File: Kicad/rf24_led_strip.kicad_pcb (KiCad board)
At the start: 2 copper layers, 50 x 50 mm, 91 parts, among them P1 12V in, P10 CONN_01X04, P11 CONN_01X07, P2 LED_OUT, P3 LED2_OUT, P4 LED3_OUT, P5 LED4_OUT, P6 LED5_OUT, P7 USB_OTG, P8 SWD, P9 UART, Q10 Q_NMOS_GDS, Q11 Q_NMOS_GDS, Q12 Q_NMOS_GDS, Q13 Q_NMOS_GDS, Q14 Q_NMOS_GDS, Q15 Q_NMOS_GDS, Q16 Q_NMOS_GDS, Q2 Q_NMOS_GDS, Q3 Q_NMOS_GDS, Q4 Q_NMOS_GDS, Q5 Q_NMOS_GDS, Q6 Q_NMOS_GDS, Q7 Q_NMOS_GDS, Q8 Q_NMOS_GDS, Q9 Q_NMOS_GDS, U1 nrf24l01+, U2 ESP-01, U3 STM32F103C8Tx, U4 AMS1117, Y1 Crystal

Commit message: Update power supply.
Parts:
- added C3: 10µF, Capacitors_SMD:C_0805, F.Cu at (106.4, 58.5)
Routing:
- net +3V3: track 123.5 -> 187.0 mm, vias 2 -> 24
- net GND: track 82.8 -> 88.6 mm, vias 21 -> 22
- net /NRST: track 21.8 -> 22.5 mm
- added copper zone on B.Cu, net +3V3
- added copper zone on F.Cu, net +3V3
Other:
- net class Dick: via_dia 0.6 -> 1.2; via_drill 0.4 -> 0.8

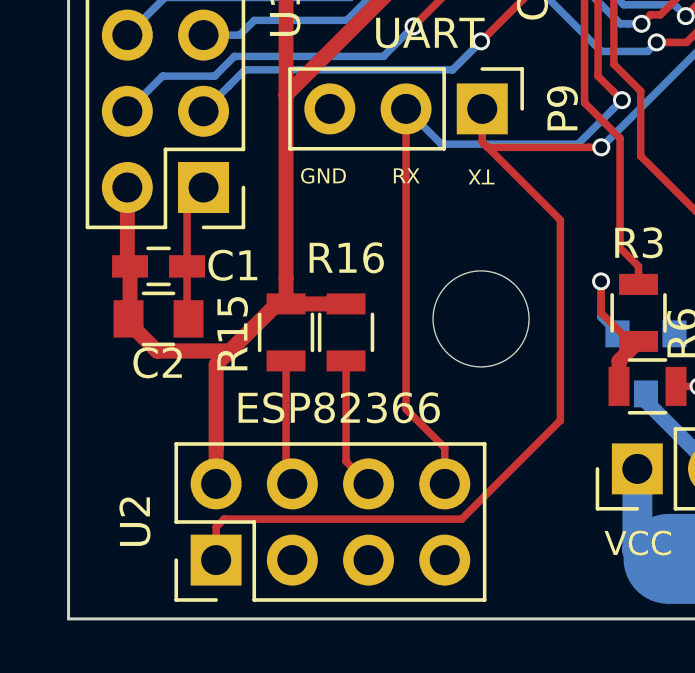
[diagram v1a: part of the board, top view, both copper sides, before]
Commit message: Add capacitors to the ESP8266.
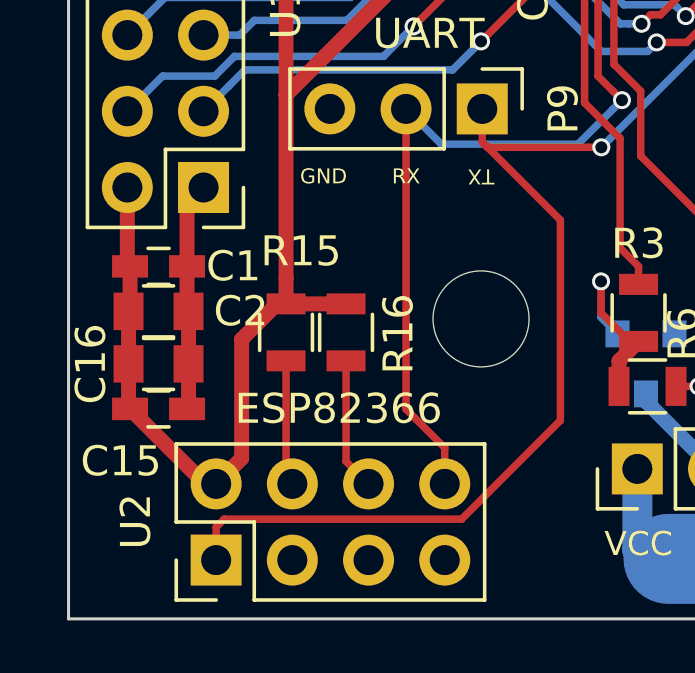
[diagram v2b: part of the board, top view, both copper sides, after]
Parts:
- added C15: 100nF, Capacitors_SMD:C_0603_HandSoldering, F.Cu at (103.0, 93.0)
- added C16: 10µF, Capacitors_SMD:C_0805, F.Cu at (103.0, 91.5)
- moved REF*** 1.00 mm to (113.0, 56.5)
- moved C2 0.25 mm to (103.0, 89.8)
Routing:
- net +3V3: track 187.0 -> 180.7 mm
- net GND: track 88.6 -> 91.7 mm
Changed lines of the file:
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@@
 (kicad_pcb (version 4) (host pcbnew 4.0.5)
   (general
-    (links 194)
-    (no_connects 0)
+    (links 198)
+    (no_connects 2)
     (area 99.949999 49.949999 150.050001 100.050001)
     (thickness 1.6)
     (drawings 52)
-    (tracks 775)
+    (tracks 777)
     (zones 0)
-    (modules 92)
+    (modules 94)
     (nets 79)
   )
@@
   )
   (setup
-    (last_trace_width 0.25)
+    (last_trace_width 0.5)
     (user_trace_width 0.25)
     (user_trace_width 0.5)
@@
     (tags "resistor 0805")
     (attr smd)
-    (fp_text reference R15 (at -0.05 -1.75 270) (layer F.SilkS)
+    (fp_text reference R15 (at 2.7 0.5 360) (layer F.SilkS)
       (effects (font (size 1 1) (thickness 0.15)))
     )
@@
     (tags "resistor 0805")
     (attr smd)
-    (fp_text reference R16 (at 2.45 0 180) (layer F.SilkS)
+    (fp_text reference R16 (at -0.05 1.75 90) (layer F.SilkS)
       (effects (font (size 1 1) (thickness 0.15)))
     )
@@
   )
   (module Capacitors_SMD:C_0805 (layer F.Cu)
-    (at 103 90)
+    (at 103 89.75)
     (descr "Capacitor SMD 0805, reflow soldering, AVX (see smccp.pdf)")
     (tags "capacitor 0805")
     (attr smd)
-    (fp_text reference C2 (at 0 1.5) (layer F.SilkS)
+    (fp_text reference C2 (at 2.75 0) (layer F.SilkS)
       (effects (font (size 1 1) (thickness 0.15)))
     )
@@
   )
   (module Symbols:OSHW-Logo2_14.6x12mm_SilkScreen (layer B.Cu)
-    (at 114 56.5)
+    (at 113 56.5)
     (descr "Open Source Hardware Symbol")
     (tags "Logo Symbol OSHW")
@@
     )
   )
+  (module Capacitors_SMD:C_0603_HandSoldering (layer F.Cu)
+    (at 103 93)
+    (descr "Capacitor SMD 0603, hand soldering")
+    (tags "capacitor 0603")
+    (attr smd)
+    (fp_text reference C15 (at -1.25 1.75) (layer F.SilkS)
+      (effects (font (size 1 1) (thickness 0.15)))
+    )
+    (fp_text value 100nF (at 0 1.5) (layer F.Fab)
+      (effects (font (size 1 1) (thickness 0.15)))
+    )
+    (fp_text user %R (at 0 -1.25) (layer F.Fab)
+      (effects (font (size 1 1) (thickness 0.15)))
+    )
+    (fp_line (start -0.8 0.4) (end -0.8 -0.4) (layer F.Fab) (width 0.1))
+    (fp_line (start 0.8 0.4) (end -0.8 0.4) (layer F.Fab) (width 0.1))
+    (fp_line (start 0.8 -0.4) (end 0.8 0.4) (layer F.Fab) (width 0.1))
+    (fp_line (start -0.8 -0.4) (end 0.8 -0.4) (layer F.Fab) (width 0.1))
+    (fp_line (start -0.35 -0.6) (end 0.35 -0.6) (layer F.SilkS) (width 0.12))
+    (fp_line (start 0.35 0.6) (end -0.35 0.6) (layer F.SilkS) (width 0.12))
+    (fp_line (start -1.8 -0.65) (end 1.8 -0.65) (layer F.CrtYd) (width 0.05))
+    (fp_line (start -1.8 -0.65) (end -1.8 0.65) (layer F.CrtYd) (width 0.05))
+    (fp_line (start 1.8 0.65) (end 1.8 -0.65) (layer F.CrtYd) (width 0.05))
+    (fp_line (start 1.8 0.65) (end -1.8 0.65) (layer F.CrtYd) (width 0.05))
+    (pad 1 smd rect (at -0.95 0) (size 1.2 0.75) (layers F.Cu F.Paste F.Mask)
+      (net 3 +3V3))
+    (pad 2 smd rect (at 0.95 0) (size 1.2 0.75) (layers F.Cu F.Paste F.Mask)
+      (net 1 GND))
+    (model Capacitors_SMD.3dshapes/C_0603.wrl
+      (at (xyz 0 0 0))
+      (scale (xyz 1 1 1))
+      (rotate (xyz 0 0 0))
+    )
+  )
+  (module Capacitors_SMD:C_0805 (layer F.Cu)
+    (at 103 91.5)
+    (descr "Capacitor SMD 0805, reflow soldering, AVX (see smccp.pdf)")
+    (tags "capacitor 0805")
+    (attr smd)
+    (fp_text reference C16 (at -2.25 0 270) (layer F.SilkS)
+      (effects (font (size 1 1) (thickness 0.15)))
+    )
+    (fp_text value 10µF (at 0 1.75) (layer F.Fab)
+      (effects (font (size 1 1) (thickness 0.15)))
+    )
+    (fp_text user %R (at 0 -1.5) (layer F.Fab)
+      (effects (font (size 1 1) (thickness 0.15)))
+    )
+    (fp_line (start -1 0.62) (end -1 -0.62) (layer F.Fab) (width 0.1))
+    (fp_line (start 1 0.62) (end -1 0.62) (layer F.Fab) (width 0.1))
+    (fp_line (start 1 -0.62) (end 1 0.62) (layer F.Fab) (width 0.1))
+    (fp_line (start -1 -0.62) (end 1 -0.62) (layer F.Fab) (width 0.1))
+    (fp_line (start 0.5 -0.85) (end -0.5 -0.85) (layer F.SilkS) (width 0.12))
+    (fp_line (start -0.5 0.85) (end 0.5 0.85) (layer F.SilkS) (width 0.12))
+    (fp_line (start -1.75 -0.88) (end 1.75 -0.88) (layer F.CrtYd) (width 0.05))
+    (fp_line (start -1.75 -0.88) (end -1.75 0.87) (layer F.CrtYd) (width 0.05))
+    (fp_line (start 1.75 0.87) (end 1.75 -0.88) (layer F.CrtYd) (width 0.05))
+    (fp_line (start 1.75 0.87) (end -1.75 0.87) (layer F.CrtYd) (width 0.05))
+    (pad 1 smd rect (at -1 0) (size 1 1.25) (layers F.Cu F.Paste F.Mask)
+      (net 3 +3V3))
+    (pad 2 smd rect (at 1 0) (size 1 1.25) (layers F.Cu F.Paste F.Mask)
+      (net 1 GND))
+    (model Capacitors_SMD.3dshapes/C_0805.wrl
+      (at (xyz 0 0 0))
+      (scale (xyz 1 1 1))
+      (rotate (xyz 0 0 0))
+    )
+  )
   (gr_text 4 (at 134.75 78.5 90) (layer F.SilkS)
     (effects (font (size 0.8 0.8) (thickness 0.15)))
@@
     (arrow2b (pts (xy 100 45) (xy 101.126504 44.413579)))
   )
+  (segment (start 104 91.5) (end 104 92.95) (width 0.5) (layer F.Cu) (net 1))
+  (segment (start 104 92.95) (end 103.95 93) (width 0.5) (layer F.Cu) (net 1))
+  (segment (start 104 89.75) (end 104 91.5) (width 0.5) (layer F.Cu) (net 1))
+  (segment (start 103.95 88.25) (end 103.95 89.7) (width 0.5) (layer F.Cu) (net 1))
+  (segment (start 103.95 89.7) (end 104 89.75) (width 0.5) (layer F.Cu) (net 1))
+  (segment (start 103.95 88.25) (end 103.95 86.17) (width 0.5) (layer F.Cu) (net 1))
+  (segment (start 103.95 86.17) (end 104.5 85.62) (width 0.5) (layer F.Cu) (net 1))
+  (segment (start 104 88.3) (end 103.95 88.25) (width 0.5) (layer F.Cu) (net 1))
   (segment (start 117.9 74.5) (end 119.5 74.5) (width 0.25) (layer F.Cu) (net 1))
   (via (at 120 74) (size 0.6) (drill 0.4) (layers F.Cu B.Cu) (net 1))
@@
   (segment (start 124.5 76.719689) (end 124.331423 76.551112) (width 0.25) (layer F.Cu) (net 1))
   (segment (start 124.331423 76.551112) (end 124.031424 76.251113) (width 0.25) (layer F.Cu) (net 1))
-  (segment (start 103.95 88.25) (end 103.95 89.95) (width 0.25) (layer F.Cu) (net 1))
-  (segment (start 103.95 89.95) (end 104 90) (width 0.25) (layer F.Cu) (net 1))
-  (segment (start 103.95 88.25) (end 103.95 86.17) (width 0.25) (layer F.Cu) (net 1))
-  (segment (start 103.95 86.17) (end 104.5 85.62) (width 0.25) (layer F.Cu) (net 1))
   (segment (start 119.7 60.5) (end 119.7 56.7) (width 0.5) (layer F.Cu) (net 1))
   (segment (start 119.7 56.7) (end 119.5 56.5) (width 0.5) (layer F.Cu) (net 1))
@@
   (segment (start 118.96 95) (end 118.96 97.71) (width 1) (layer B.Cu) (net 2))
   (segment (start 118.96 97.71) (end 119.25 98) (width 1) (layer B.Cu) (net 2))
+  (segment (start 104.92 95.5) (end 105.769999 94.650001) (width 0.5) (layer F.Cu) (net 3))
+  (segment (start 105.769999 94.650001) (end 105.769999 90.680001) (width 0.5) (layer F.Cu) (net 3))
+  (segment (start 105.769999 90.680001) (end 106.95 89.5) (width 0.5) (layer F.Cu) (net 3))
+  (segment (start 106.95 89.5) (end 107.25 89.5) (width 0.5) (layer F.Cu) (net 3))
+  (segment (start 102.05 93) (end 104.55 95.5) (width 0.5) (layer F.Cu) (net 3))
+  (segment (start 104.55 95.5) (end 104.92 95.5) (width 0.5) (layer F.Cu) (net 3))
+  (segment (start 102 91.5) (end 102 92.95) (width 0.5) (layer F.Cu) (net 3))
+  (segment (start 102 92.95) (end 102.05 93) (width 0.5) (layer F.Cu) (net 3))
+  (segment (start 102 89.75) (end 102 91.5) (width 0.5) (layer F.Cu) (net 3))
+  (segment (start 102.05 88.25) (end 102.05 89.7) (width 0.5) (layer F.Cu) (net 3))
+  (segment (start 102.05 89.7) (end 102 89.75) (width 0.5) (layer F.Cu) (net 3))
   (segment (start 119.175004 70.75) (end 119.05 70.75) (width 0.25) (layer F.Cu) (net 3))
   (segment (start 120.75 74) (end 120.75 72.324996) (width 0.25) (layer F.Cu) (net 3))
@@
   (segment (start 110 62.75) (end 109.549999 63.200001) (width 0.5) (layer B.Cu) (net 3))
   (via (at 107.25 75) (size 1.2) (drill 0.8) (layers F.Cu B.Cu) (net 3))
-  (segment (start 107.25 89.5) (end 106.95 89.5) (width 0.5) (layer F.Cu) (net 3))
-  (segment (start 104.92 91.53) (end 104.92 94.297919) (width 0.5) (layer F.Cu) (net 3))
-  (segment (start 106.95 89.5) (end 104.92 91.53) (width 0.5) (layer F.Cu) (net 3))
-  (segment (start 104.92 94.297919) (end 104.92 95.5) (width 0.5) (layer F.Cu) (net 3))
   (segment (start 102 90) (end 102 90.125) (width 0.5) (layer F.Cu) (net 3))
-  (segment (start 102 90.125) (end 102.950001 91.075001) (width 0.5) (layer F.Cu) (net 3))
-  (segment (start 102.950001 91.075001) (end 105.374999 91.075001) (width 0.5) (layer F.Cu) (net 3))
-  (segment (start 105.374999 91.075001) (end 106.95 89.5) (width 0.5) (layer F.Cu) (net 3))
-  (segment (start 102.05 88.25) (end 102.05 89.95) (width 0.5) (layer F.Cu) (net 3))
   (segment (start 102.05 89.95) (end 102 90) (width 0.5) (layer F.Cu) (net 3))
   (segment (start 101.96 85.62) (end 101.96 88.16) (width 0.5) (layer F.Cu) (net 3))
@@
   (segment (start 109.65 60.75) (end 109 60.75) (width 0.25) (layer F.Cu) (net 3))
   (via (at 109 60.75) (size 0.6) (drill 0.4) (layers F.Cu B.Cu) (net 3))
-  (segment (start 105.499999 90.950001) (end 105.95 90.5) (width 0.25) (layer F.Cu) (net 3))
-  (segment (start 105.95 90.5) (end 106.95 89.5) (width 0.25) (layer F.Cu) (net 3))
-  (segment (start 104.92 91.53) (end 105.95 90.5) (width 0.25) (layer F.Cu) (net 3))
-  (segment (start 102 90.125) (end 102.825001 90.950001) (width 0.25) (layer F.Cu) (net 3))
-  (segment (start 102.825001 90.950001) (end 105.499999 90.950001) (width 0.25) (layer F.Cu) (net 3))
   (segment (start 133 67.25) (end 134 66.25) (width 0.25) (layer F.Cu) (net 3))
   (segment (start 134 66.25) (end 135.6 66.25) (width 0.25) (layer F.Cu) (net 3))
